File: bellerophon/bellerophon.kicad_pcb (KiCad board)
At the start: 2 copper layers, 55 x 98 mm, 34 parts, among them Q1 ST3413A, Q2 IRLL014NPBF, Q3 IRLL014NPBF, U1 HT7350-A, U2 Adafruit_ICM20948, U3 MPL3115A2, U4 Teensy4.0, U5 Adafruit SPI Flash SD Card

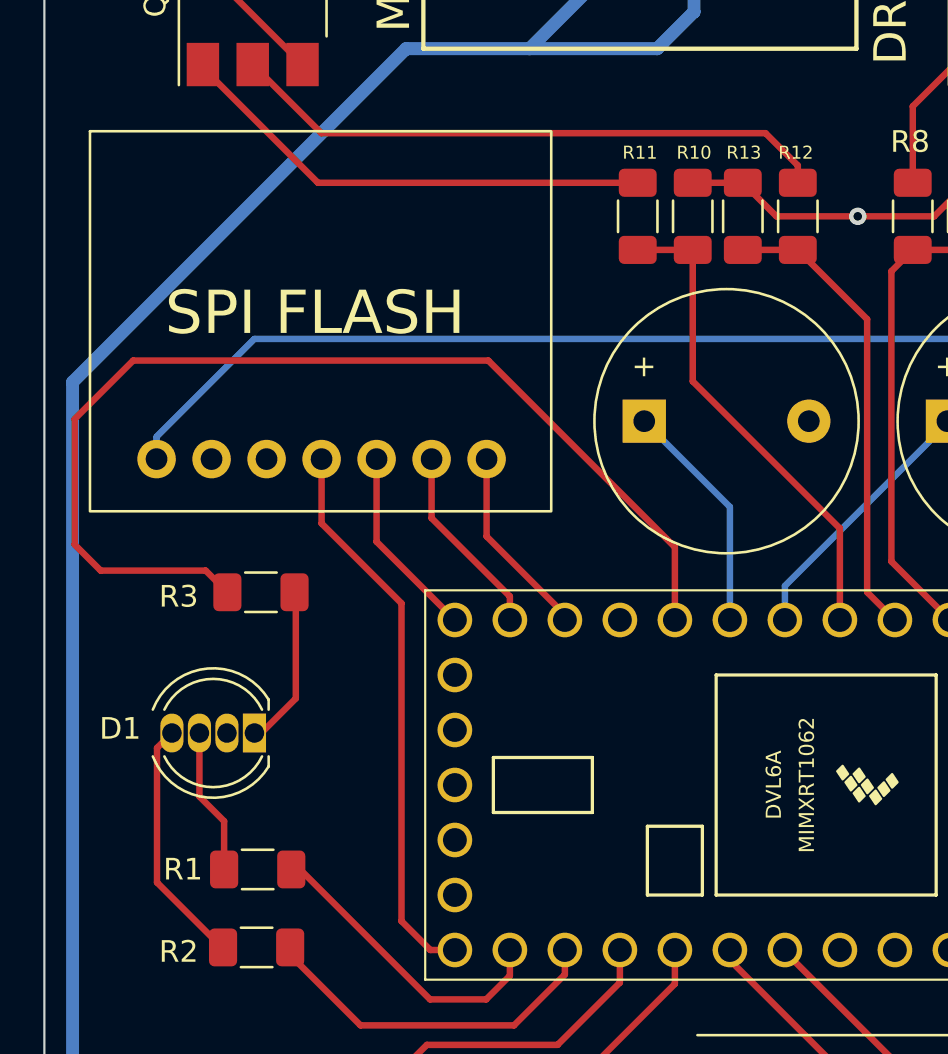
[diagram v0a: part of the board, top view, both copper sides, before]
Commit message: create footprint for xtsd and add to pcb
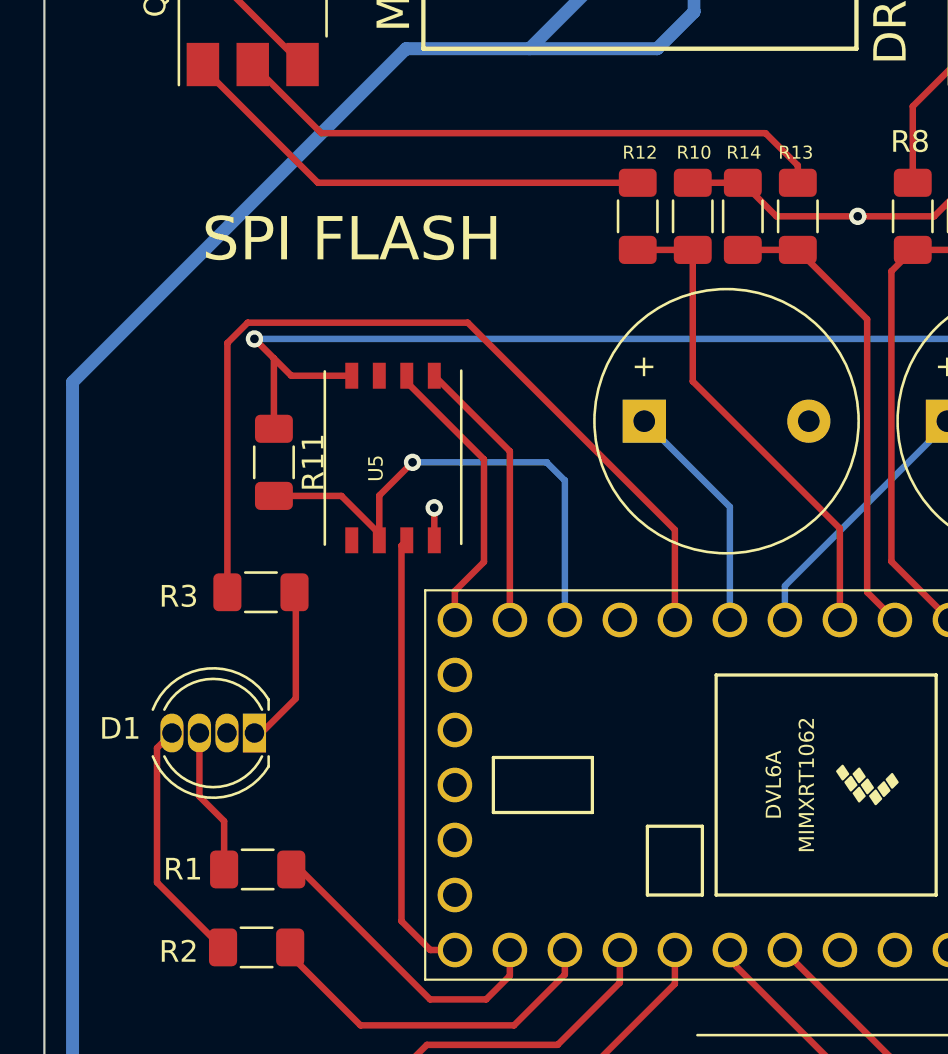
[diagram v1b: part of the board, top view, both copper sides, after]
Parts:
- added R11: 10k ohms, Resistor_SMD:R_1206_3216Metric_Pad1.30x1.75mm_HandSolder, F.Cu at (135.6, 77.4)
- U5: value Adafruit SPI Flash SD Card -> XTSD; footprint Adafruit:SD-CARD-B21.59x17.78mm-1X07_ROUND_70-P2.5mm -> XTSD:LGA8_8X6
- moved U5 7.11 mm to (141.1, 77.2), turned to 90 degrees
- renumbered R11 to R12, R12 to R13, R13 to R14
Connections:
- U5 pad 1: +3.3V -> unconnected-(U5-Pad1)
- U5 pad 2: unconnected-(U5-Pad2) -> /CS
- U5 pad 3: GND -> /SCK
- U5 pad 4: /SCK -> GND
- U5 pad 5: /MISO -> /MOSI
- U5 pad 6: /MOSI -> /MISO
- U5 pad 7: /CS -> unconnected-(U5-Pad7)
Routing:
- net /CS: track 8.93 -> 24.2 mm, vias 0 -> 1
- net RGB3: track 49.5 -> 40.7 mm
- net /SCK: track 25.9 -> 20.7 mm
- net /MISO: track 8.93 -> 13.3 mm
- net /MOSI: track 8.93 -> 12.7 mm
- net GND: track 74.3 -> 75.8 mm, vias 3 -> 4
- net +3.3V: track 162.9 -> 163.9 mm, vias 0 -> 1

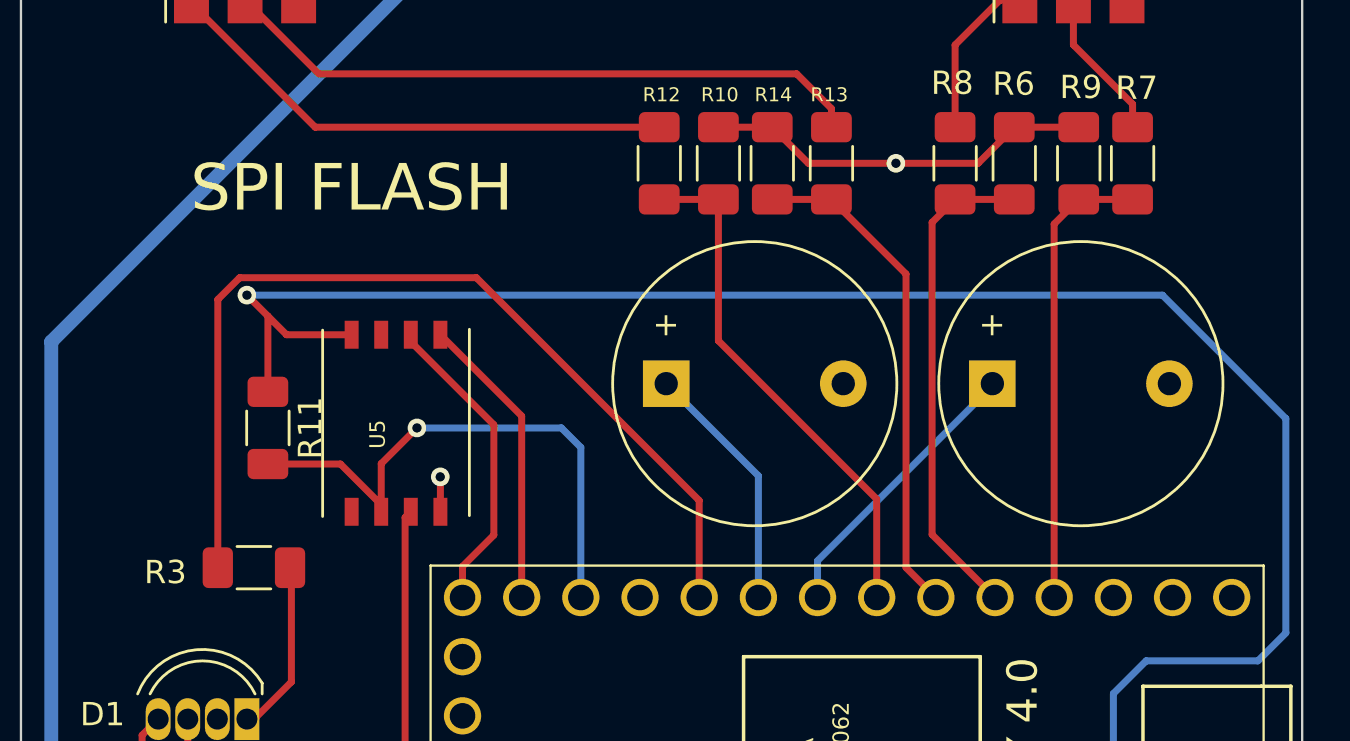
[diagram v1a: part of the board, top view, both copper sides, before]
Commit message: remove second buzzer
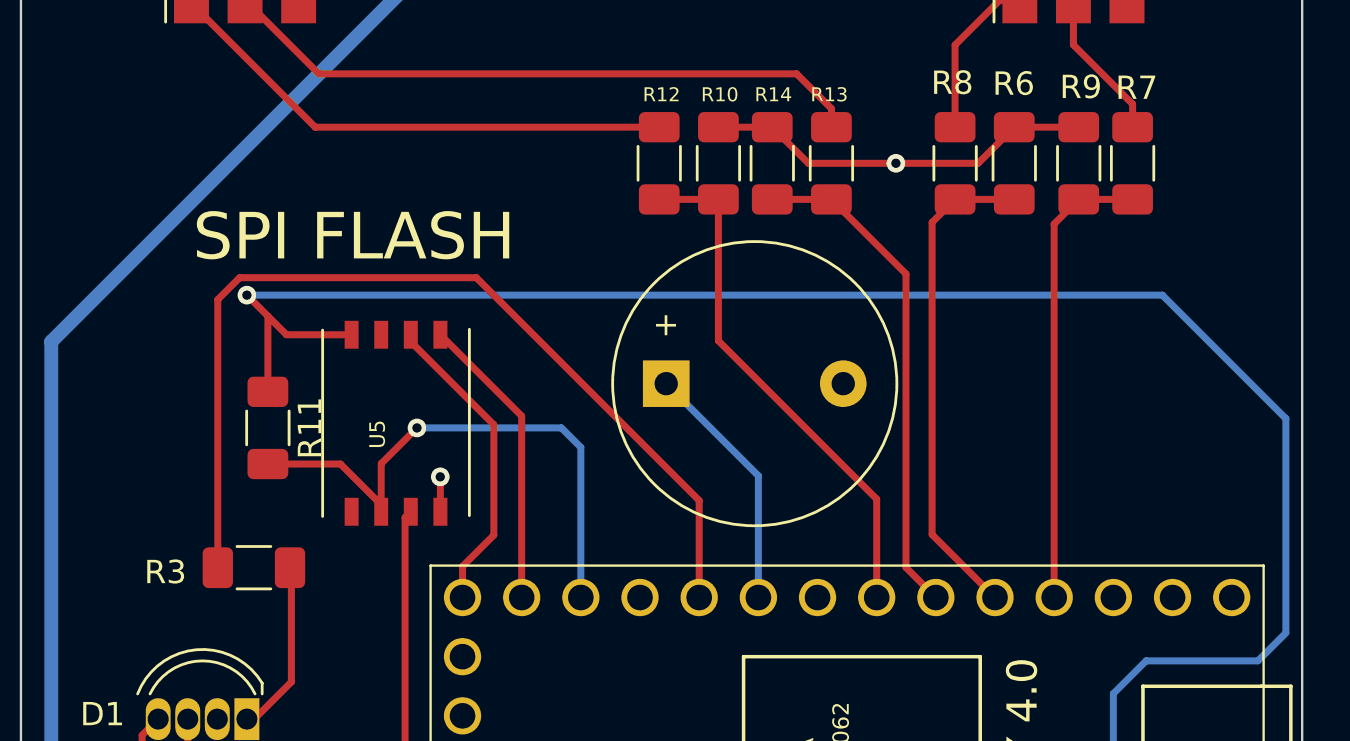
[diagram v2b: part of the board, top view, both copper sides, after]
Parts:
- removed BZ2: Buzzer, Buzzer:PiezoBuzzer-PS1240
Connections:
- U4 pad 8: BZR2 -> unconnected-(U4-Pad8)
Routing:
- net BZR2: track 12.2 -> 0.00 mm
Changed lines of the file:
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@@
   (net 46 "Net-(PYRO1-Pad4)")
   (net 47 "BZR1")
-  (net 48 "BZR2")
+  (net 48 "unconnected-(U4-Pad8)")
   (net 49 "BATT+")
   (net 50 "unconnected-(U4-Pad2)")
@@
       (net 24 "PY2_TEST") (pintype "passive"))
     (model "${KICAD6_3DMODEL_DIR}/Resistor_SMD.3dshapes/R_1206_3216Metric.wrl"
-      (offset (xyz 0 0 0))
-      (scale (xyz 1 1 1))
-      (rotate (xyz 0 0 0))
-    )
-  )
-  (footprint "Buzzer:PiezoBuzzer-PS1240" (layer "F.Cu")
-    (at 166.7 75.5)
-    (descr "Generic Buzzer, D12mm height 9.5mm with RM7.6mm")
-    (tags "buzzer")
-    (property "Sheetfile" "bellerophon.kicad_sch")
-    (property "Sheetname" "")
-    (attr through_hole)
-    (fp_text reference "BZ2" (at 3.8 -7.2) (layer "F.SilkS") hide
-      (effects (font (size 1 1) (thickness 0.15)))
-    )
-    (fp_text value "Buzzer" (at 3.8 3.25) (layer "F.Fab")
-      (effects (font (size 1 1) (thickness 0.15)))
-    )
-    (fp_text user "+" (at -0.01 -2.54) (layer "F.SilkS")
-      (effects (font (size 1 1) (thickness 0.15)))
-    )
-    (fp_text user "+" (at -0.01 -2.54) (layer "F.Fab")
-      (effects (font (size 1 1) (thickness 0.15)))
-    )
-    (fp_text user "${REFERENCE}" (at 3.8 -4) (layer "F.Fab")
-      (effects (font (size 1 1) (thickness 0.15)))
-    )
-    (fp_circle (center 3.8 0) (end 9.9 0) (layer "F.SilkS") (width 0.12) (fill none))
-    (fp_circle (center 3.8 0) (end 10.05 0) (layer "F.CrtYd") (width 0.05) (fill none))
-    (fp_circle (center 3.8 0) (end 9.8 0) (layer "F.Fab") (width 0.1) (fill none))
-    (fp_circle (center 3.8 0) (end 4.8 0) (layer "F.Fab") (width 0.1) (fill none))
-    (pad "1" thru_hole rect (at 0 0) (size 2 2) (drill 1) (layers *.Cu *.Mask)
-      (net 48 "BZR2") (pinfunction "-") (pintype "passive"))
-    (pad "2" thru_hole circle (at 7.6 0) (size 2 2) (drill 1) (layers *.Cu *.Mask)
-      (net 1 "GND") (pinfunction "+") (pintype "passive"))
-    (model "${KICAD6_3DMODEL_DIR}/Buzzer_Beeper.3dshapes/Buzzer_12x9.5RM7.6.wrl"
       (offset (xyz 0 0 0))
       (scale (xyz 1 1 1))
@@
       ) (layer "F.Fab") (width 0) (fill solid))
     (pad "1" smd rect (at -3.8 -1.905) (size 0.6 1.2) (layers "F.Cu" "F.Paste" "F.Mask")
-      (net 54 "unconnected-(U5-Pad1)") (pinfunction "SD2") (pintype "bidirectional") (solder_mask_margin 0.0508))
+      (net 54 "unconnected-(U5-Pad1)") (pinfunction "SD2") (pintype "bidirectional+no_connect") (solder_mask_margin 0.0508))
     (pad "2" smd rect (at -3.8 -0.635) (size 0.6 1.2) (layers "F.Cu" "F.Paste" "F.Mask")
       (net 33 "/CS") (pinfunction "SSEL/SD3") (pintype "bidirectional") (solder_mask_margin 0.0508))
@@
       (net 44 "/MISO") (pinfunction "MISO/SD0") (pintype "bidirectional") (solder_mask_margin 0.0508))
     (pad "7" smd rect (at 3.8 -0.635) (size 0.6 1.2) (layers "F.Cu" "F.Paste" "F.Mask")
-      (net 55 "unconnected-(U5-Pad7)") (pinfunction "SD1") (pintype "bidirectional") (solder_mask_margin 0.0508))
+      (net 55 "unconnected-(U5-Pad7)") (pinfunction "SD1") (pintype "bidirectional+no_connect") (solder_mask_margin 0.0508))
     (pad "8" smd rect (at 3.8 -1.905) (size 0.6 1.2) (layers "F.Cu" "F.Paste" "F.Mask")
       (net 6 "+3.3V") (pinfunction "VCC") (pintype "power_in") (solder_mask_margin 0.0508))
@@
       (net 23 "PY2") (pinfunction "5_IN2") (pintype "bidirectional"))
     (pad "8" thru_hole circle (at 1.27 7.62 180) (size 1.6 1.6) (drill 1.1) (layers *.Cu *.Mask)
-      (net 48 "BZR2") (pinfunction "6_OUT1D") (pintype "bidirectional"))
+      (net 48 "unconnected-(U4-Pad8)") (pinfunction "6_OUT1D") (pintype "bidirectional+no_connect"))
     (pad "9" thru_hole circle (at 3.81 7.62 180) (size 1.6 1.6) (drill 1.1) (layers *.Cu *.Mask)
       (net 47 "BZR1") (pinfunction "7_RX2_OUT1A") (pintype "bidirectional"))
@@
     (effects (font (size 1.5 1.5) (thickness 0.25)))
   )
-  (gr_text "SPI FLASH\n" (at 139.2 67.1) (layer "F.SilkS")
+  (gr_text "SPI FLASH\n" (at 139.3 69.2) (layer "F.SilkS")
     (effects (font (size 2 2) (thickness 0.3)))
   )
@@
   (segment (start 156.655 84.68) (end 156.655 79.455) (width 0.3) (layer "B.Cu") (net 47))
   (segment (start 156.655 79.455) (end 152.7 75.5) (width 0.3) (layer "B.Cu") (net 47))
-  (segment (start 159.195 83.105) (end 166.7 75.6) (width 0.3) (layer "B.Cu") (net 48))
-  (segment (start 159.195 84.68) (end 159.195 83.105) (width 0.3) (layer "B.Cu") (net 48))
   (segment (start 166.55 135.5625) (end 166.55 133.65) (width 0.6) (layer "F.Cu") (net 49))
   (segment (start 149.9375 130.4375) (end 148.4 128.9) (width 0.6) (layer "F.Cu") (net 49))
